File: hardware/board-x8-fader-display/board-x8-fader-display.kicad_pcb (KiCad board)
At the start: 2 copper layers, 250 x 210 mm, 50 parts, among them J1 OLED0, J2 OLED1, J3 OLED2, J4 OLED3, J5 OLED4, J6 OLED5, J7 OLED6, J8 OLED7, J9 Conn_02x16_Odd_Even, U1 74xx138, U10 74xx238, U2 74xx138, U3 L293, U4 L293, U5 L293, U6 L293, U7 CAP1296, U8 CAP1296, U9 4051

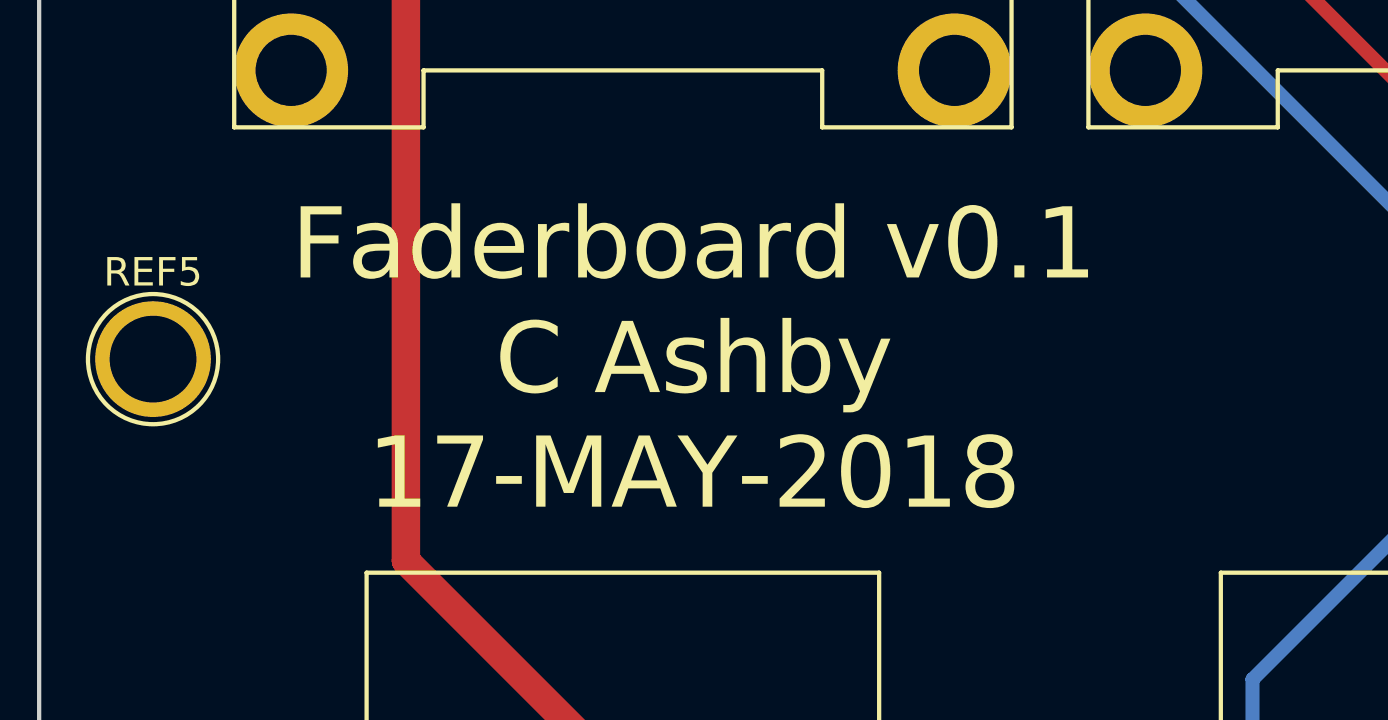
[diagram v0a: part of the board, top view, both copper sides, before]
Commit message: Tidying board output file locations, corrected silkscreen for v1.0 fader board (not fabbed)
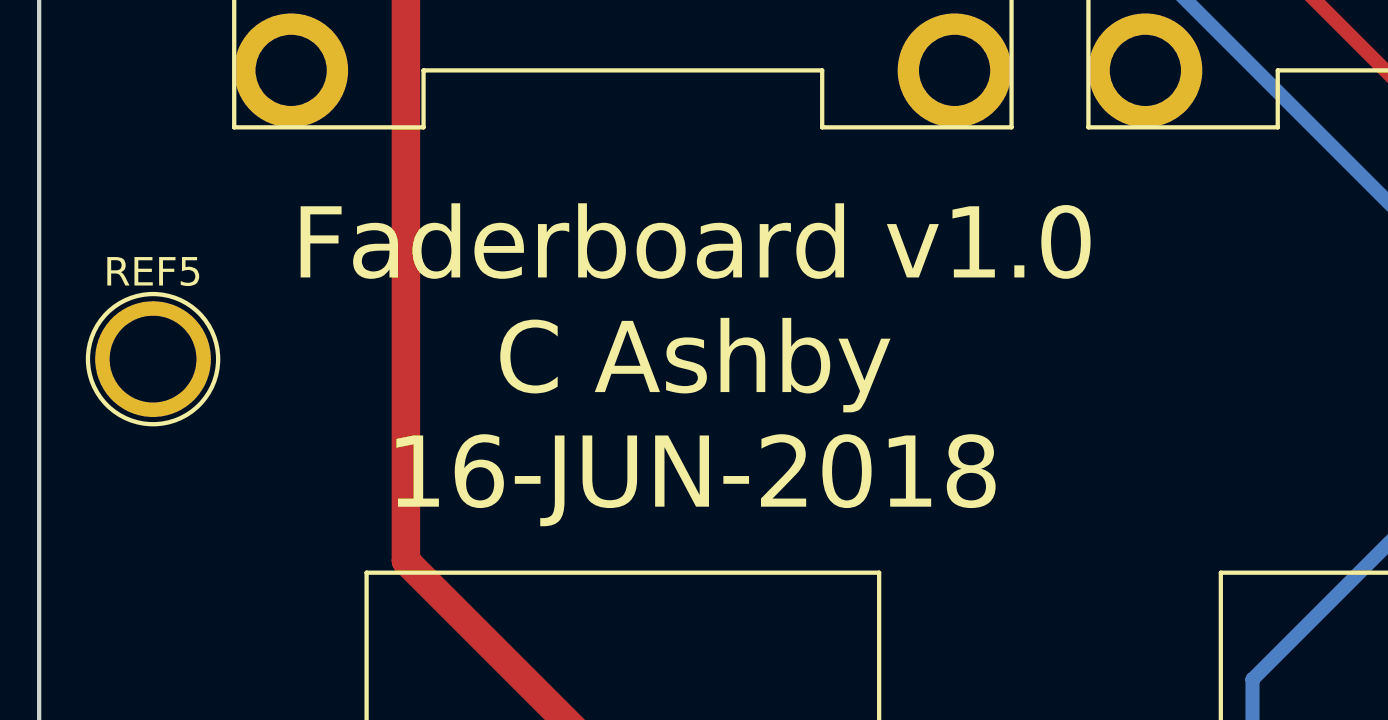
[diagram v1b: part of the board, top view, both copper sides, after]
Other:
- board text added: "Faderboard v1.0 C Ashby 16-JUN-2018"
- board text removed: "Faderboard v0.1 C Ashby 17-MAY-2018"
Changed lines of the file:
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@@
   (gr_line (start 334.5 29) (end 334.5 239) (angle 90) (layer Edge.Cuts) (width 0.15))
   (gr_line (start 84.5 29) (end 334.5 29) (angle 90) (layer Edge.Cuts) (width 0.15))
-  (gr_text "Faderboard v0.1\nC Ashby\n17-MAY-2018" (at 107.5 75) (layer F.SilkS)
+  (gr_text "Faderboard v1.0\nC Ashby\n16-JUN-2018" (at 107.5 75) (layer F.SilkS)
     (effects (font (size 2.5 2.5) (thickness 0.3)))
   )
